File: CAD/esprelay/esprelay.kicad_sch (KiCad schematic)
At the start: 7 parts

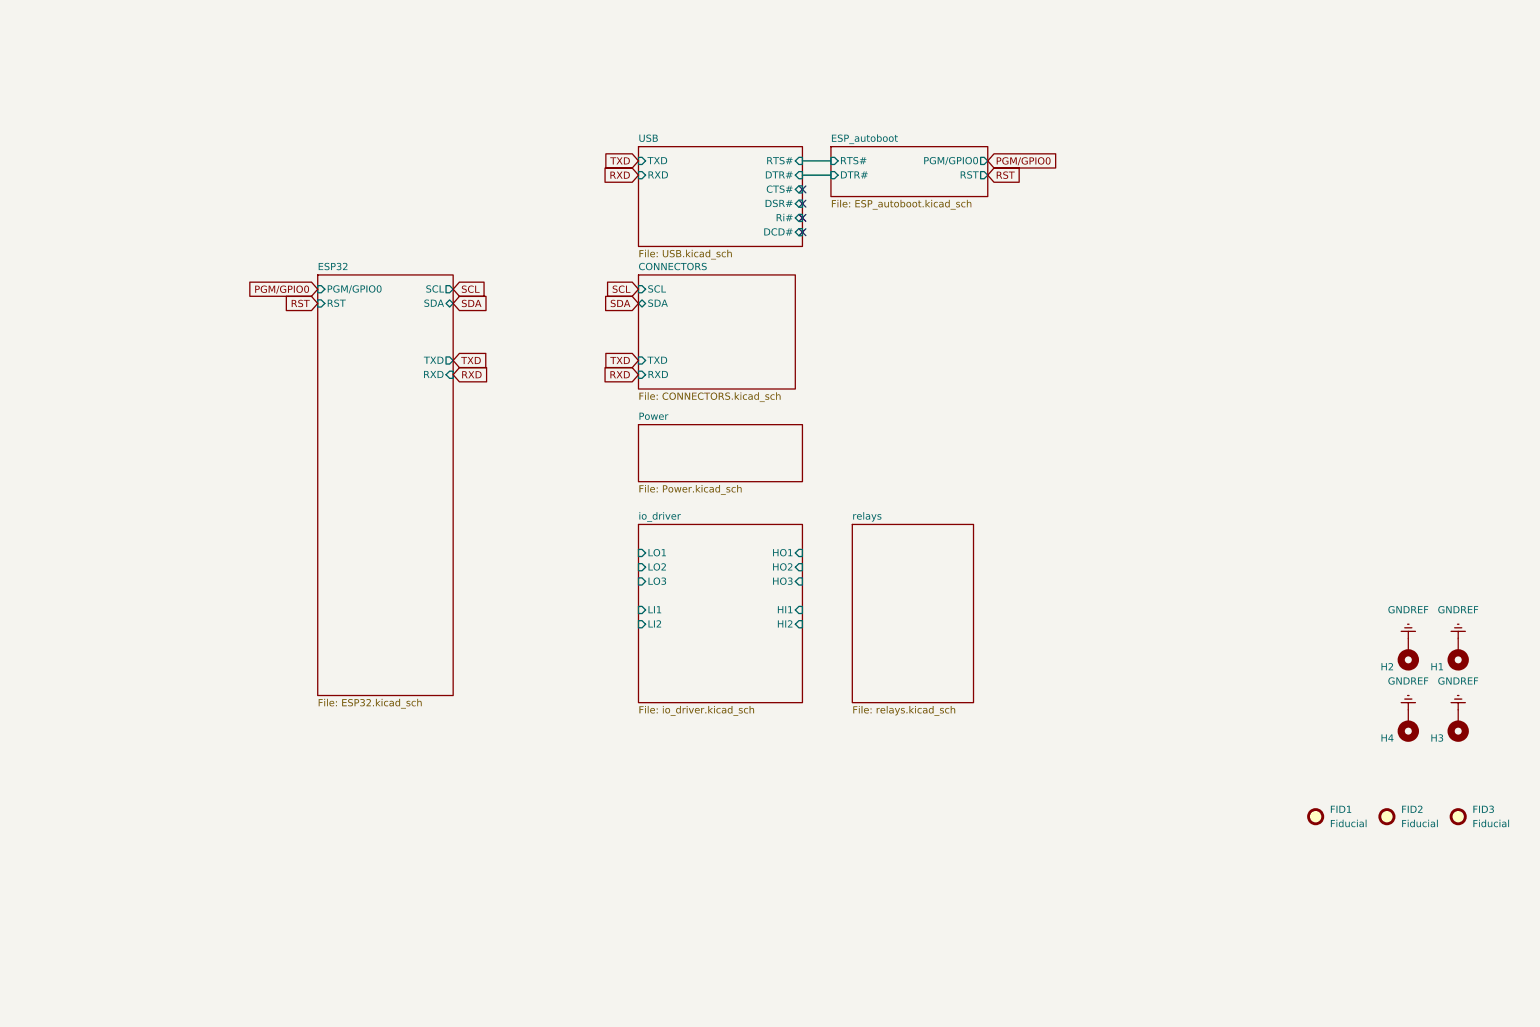
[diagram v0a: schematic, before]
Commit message: Feat: Changed module to ESP12F
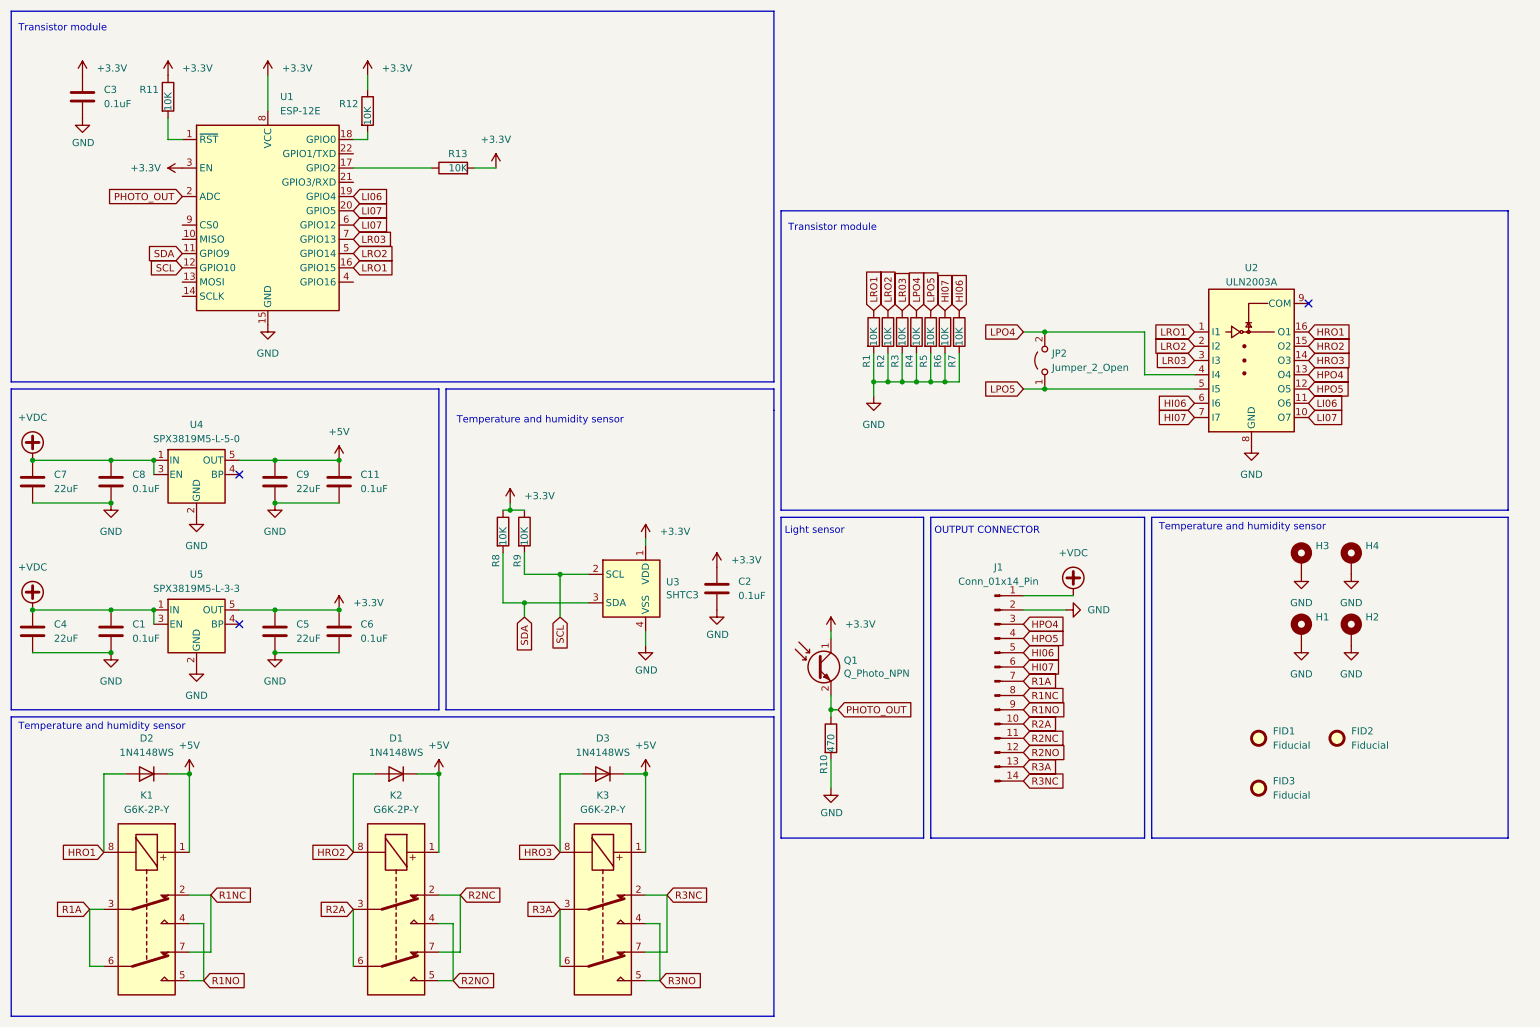
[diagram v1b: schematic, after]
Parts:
- added C1, C11, C2, C3, C6, C8: 0.1uF, Capacitor_SMD:C_0603_1608Metric, symbol Device:C
- added C4, C5, C7, C9: 22uF, Capacitor_SMD:C_0603_1608Metric, symbol Device:C
- added D1, D2, D3: 1N4148WS, Diode_SMD:D_SOD-323, symbol Diode:1N4148WS
- added J1: Conn_01x14_Pin, symbol Connector:Conn_01x14_Pin
- added JP2: Jumper_2_Open, Jumper:SolderJumper-2_P1.3mm_Open_TrianglePad1.0x1.5mm, symbol Jumper:Jumper_2_Open
- added K1, K2, K3: G6K-2P-Y, Relay_THT:Relay_DPDT_Omron_G6K-2P-Y, symbol Relay:G6K-2
- added Q1: Q_Photo_NPN, snapeda:TR8, symbol Device:Q_Photo_NPN
- added R1, R11, R12, R13, R2, R3, R4, R5, R6, R7, R8, R9: 10K, symbol Device:R
- added R10: 470, symbol Device:R
- added U1: ESP-12E, RF_Module:ESP-12E, symbol RF_Module:ESP-12E
- added U2: ULN2003A, Package_SO:SOIC-16_3.9x9.9mm_P1.27mm, symbol Transistor_Array:ULN2003A
- added U3: SHTC3, kicad:Sensirion_DFN-4-1EP_2x2mm_P1mm_EP0.7x1.6mm, symbol Sensor_Humidity:SHTC3
- added U4: SPX3819M5-L-5-0, Package_TO_SOT_SMD:SOT-23-5, symbol Regulator_Linear:SPX3819M5-L-5-0
- added U5: SPX3819M5-L-3-3, Package_TO_SOT_SMD:SOT-23-5, symbol Regulator_Linear:SPX3819M5-L-3-3
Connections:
- net SCL: now also R9.2, U1.12 (GPIO10), U3.2 (SCL)
- net SDA: now also R8.2, U1.11 (GPIO9), U3.3 (SDA)
- net GNDREF renamed GND
- net GND: now also C1.1, C11.2, C2.2, C3.2, C4.2, C5.2, C6.2, C7.2, C8.1, C9.2, J1.2 (Pin_2), R1.2, R10.2, R2.2, R3.2, R4.2, R5.2, R6.2, R7.2, U1.15 (GND), U2.8 (GND), U3.4 (VSS), U4.2 (GND), U5.2 (GND)
- new net: R11.2, U1.1 (~{RST})
- new net: R13.1, U1.17 (GPIO2)
- new net: R12.2, U1.18 (GPIO0)
- new net +3.3V: C2.1, C3.1, C5.1, C6.1, Q1.1 (C), R11.1, R12.1, R13.2, R8.1, R9.1, U1.3 (EN), U1.8 (VCC), U3.1 (VDD), U5.5 (OUT)
- new net +5V: C11.1, C9.1, D1.1 (K), D2.1 (K), D3.1 (K), K1.1, K2.1, K3.1, U4.5 (OUT)
- new net +VDC: C1.2, C4.1, C7.1, C8.2, J1.1 (Pin_1), U4.1 (IN), U4.3 (EN), U5.1 (IN), U5.3 (EN)
- new net HI06: J1.5 (Pin_5), R7.1, U2.6 (I6)
- new net HI07: J1.6 (Pin_6), R6.1, U2.7 (I7)
- new net HPO4: J1.3 (Pin_3), U2.13 (O4)
- new net HPO5: J1.4 (Pin_4), U2.12 (O5)
- new net HRO1: D2.2 (A), K1.8, U2.16 (O1)
- new net HRO2: D1.2 (A), K2.8, U2.15 (O2)
- new net HRO3: D3.2 (A), K3.8, U2.14 (O3)
- new net LI06: U1.19 (GPIO4), U2.11 (O6)
- new net LI07: U1.20 (GPIO5), U1.6 (GPIO12), U2.10 (O7)
- new net LPO4: JP2.2 (B), R4.1, U2.4 (I4)
- new net LPO5: JP2.1 (A), R5.1, U2.5 (I5)
- new net LR03: R3.1, U1.7 (GPIO13), U2.3 (I3)
- new net LRO1: R1.1, U1.16 (GPIO15), U2.1 (I1)
- new net LRO2: R2.1, U1.5 (GPIO14), U2.2 (I2)
- new net PHOTO_OUT: Q1.2 (E), R10.1, U1.2 (ADC)
- new net R1A: J1.7 (Pin_7), K1.3, K1.6
- new net R1NC: J1.8 (Pin_8), K1.2, K1.7
- new net R1NO: J1.9 (Pin_9), K1.4, K1.5
- new net R2A: J1.10 (Pin_10), K2.3, K2.6
- new net R2NC: J1.11 (Pin_11), K2.2, K2.7
- new net R2NO: J1.12 (Pin_12), K2.4, K2.5
- new net R3A: J1.13 (Pin_13), K3.3, K3.6
- new net R3NC: J1.14 (Pin_14), K3.2, K3.7
- new net R3NO: K3.4, K3.5
- no-connect marks 4 -> 3
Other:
- removed sheet CONNECTORS
- removed sheet ESP32
- removed sheet ESP_autoboot
- removed sheet Power
- removed sheet USB
- removed sheet io_driver
- removed sheet relays
- note added: "Light sensor"
- note added: "OUTPUT CONNECTOR"
- note added: "Temperature and humidity sensor"
- note added: "Transistor module"
- moved on the sheet: FID1, FID2, FID3, H1, H2, H3, H4

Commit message: Feat: Started Routing
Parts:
- removed JP2: Jumper_2_Open, Jumper:SolderJumper-2_P1.3mm_Open_TrianglePad1.0x1.5mm, symbol Jumper:Jumper_2_Open
- removed U1: ESP-12E, RF_Module:ESP-12E, symbol RF_Module:ESP-12E
- added J2: Conn_01x06_Pin, TestPoint:TestPoint_Pad_1.0x1.0mm_6pad, symbol Connector:Conn_01x06_Pin
- added JP1: Jumper_2_Open, Jumper:SolderJumper-2_P1.3mm_Open_TrianglePad1.0x1.5mm, symbol Jumper:Jumper_2_Open
- added U1: ESP-12F, RF_Module:ESP-12E, symbol RF_Module:ESP-12F
- J1: footprint (none) -> Connector_JST:JST_GH_SM12B-GHS-TB_1x12-1MP_P1.25mm_Horizontal
- R1, R10, R11, R12, R13, R2, R3, R4, R5, R6, R7, R8, R9: footprint (none) -> Resistor_SMD:R_0603_1608Metric
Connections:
- net +3.3V: now also J2.1 (Pin_1), JP1.2 (B), U1.3 (EN), U1.8 (VCC)
- net GND: now also J1.13 (Pin_13), J1.14 (Pin_14), J2.6 (Pin_6), U1.15 (GND)
- net HI06: now also J1.4 (Pin_4); no longer J1.5 (Pin_5)
- net HI07: now also J1.5 (Pin_5); no longer J1.6 (Pin_6)
- net LI06: now also U1.6 (GPIO12)
- net LI07: now also U1.20 (GPIO5)
- net LPO4: no longer U2.4 (I4)
- net LPO5: no longer U2.5 (I5)
- net LR03: now also U1.7 (GPIO13)
- net LRO1: now also U1.16 (GPIO15)
- net LRO2: now also U1.5 (GPIO14)
- net PHOTO_OUT: now also U1.2 (ADC)
- net R1A: now also J1.6 (Pin_6); no longer J1.7 (Pin_7)
- net R1NC: now also J1.7 (Pin_7); no longer J1.8 (Pin_8)
- net R1NO: now also J1.8 (Pin_8); no longer J1.9 (Pin_9)
- net R2A: now also J1.9 (Pin_9); no longer J1.10 (Pin_10)
- net R2NC: now also J1.10 (Pin_10); no longer J1.11 (Pin_11)
- net R2NO: no longer J1.12 (Pin_12)
- net R3A: now also J1.11 (Pin_11); no longer J1.13 (Pin_13)
- net R3NC: no longer J1.14 (Pin_14)
- net R3NO: now also J1.12 (Pin_12)
- net SCL: now also U1.12 (GPIO10)
- net SDA: now also U1.11 (GPIO9)
- net RST: now reaches R11.2
- net RST: now also J2.5 (Pin_5), U1.1 (~{RST}), U1.4 (GPIO16)
- net at R13.1: now also U1.17 (GPIO2)
- net BOOT: now reaches R12.2
- net BOOT: now also J2.4 (Pin_4), U1.18 (GPIO0)
- net +5V renamed VBUS
- net VBUS: now also JP1.1 (A)
- net HPO4 renamed HP45
- net HP45: now also U2.12 (O5); no longer J1.3 (Pin_3)
- removed net HPO5: J1.4 (Pin_4), U2.12 (O5)
- new net HPO45: J1.3 (Pin_3)
- new net LP45: U1.19 (GPIO4), U2.4 (I4), U2.5 (I5)
- new net RX: J2.3 (Pin_3), U1.21 (GPIO3/RXD)
- new net TX: J2.2 (Pin_2), U1.22 (GPIO1/TXD)
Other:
- note added: "Hardware"
- note added: "Linear Regulators"
- note added: "Relays"
- moved on the sheet: R12

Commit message: Feat: Pretty much complete
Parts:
- removed H1, H4: MountingHole_Pad, MountingHole:MountingHole_2.5mm, symbol Mechanical:MountingHole_Pad
- removed H2, H3: MountingHole_Pad, MountingHole:MountingHole_2.5mm_Pad_Via, symbol Mechanical:MountingHole_Pad
- removed R5: 10K, Resistor_SMD:R_0603_1608Metric, symbol Device:R
- added SW1: SW_SPST, Button_Switch_SMD:SW_SPST_B3U-1000P, symbol Switch:SW_SPST
- JP1: footprint Jumper:SolderJumper-2_P1.3mm_Open_TrianglePad1.0x1.5mm -> Resistor_SMD:R_0603_1608Metric
- Q1: footprint snapeda:TR8 -> LED_SMD:LED_0603_1608Metric
- U4: renamed from U3; footprint kicad:Sensirion_DFN-4-1EP_2x2mm_P1mm_EP0.7x1.6mm -> Sensor_Humidity:Sensirion_DFN-4-1EP_2x2mm_P1mm_EP0.7x1.6mm
- renumbered C7 to C1, C2 to C10, C4 to C2, C8 to C4, C1 to C5, C9 to C6, C5 to C7, C11 to C8, C6 to C9, D2 to D1, D1 to D2, FID3 to FID2, FID2 to FID3, J2 to J1, J1 to J2, R11 to R1, R4 to R10, R6 to R12, R7 to R13, R12 to R2, R13 to R3, R8 to R4, R9 to R5, R10 to R6, R1 to R7, R2 to R8, R3 to R9, U4 to U1, U5 to U2, U1 to U3, U2 to U5
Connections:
- net HPO45 is gone; now on net HI1: J2.3 (Pin_3)
- net BOOT: now also SW1.1 (A)
- net GND: now also SW1.2 (B)
- net R2NC: no longer J2.10 (Pin_10)
- net R2NO: now also J2.10 (Pin_10)
- net HI06 renamed HI1
- net HI1: no longer J2.4 (Pin_4)
- net HI07 renamed HI2
- net HI2: now also J2.4 (Pin_4); no longer J2.5 (Pin_5)
- net HP45 renamed RO2
- net RO2: now also D2.2 (A), K2.8; no longer U5.12 (O5)
- net HRO1 renamed RO1
- net RO1: now also U5.14 (O3); no longer U5.16 (O1)
- removed net HRO2: D2.2 (A), K2.8, U5.15 (O2)
- net HRO3 renamed RO3
- net RO3: now also U5.12 (O5); no longer U5.14 (O3)
- net LI06 renamed GPIO12
- net GPIO12: now also R8.1, U5.3 (I3); no longer U5.11 (O6)
- net LI07 renamed GPIO15
- net GPIO15: now also U3.16 (GPIO15); no longer U3.20 (GPIO5)
- removed net LP45: U3.19 (GPIO4), U5.4 (I4), U5.5 (I5)
- net LPO4 renamed GPIO5
- net GPIO5: now also U3.20 (GPIO5), U5.5 (I5)
- removed net LR03: R9.1, U3.7 (GPIO13), U5.3 (I3)
- net LRO1 renamed GPIO13
- net GPIO13: now also U3.7 (GPIO13), U5.2 (I2); no longer U3.16 (GPIO15)
- removed net LRO2: R8.1, U3.5 (GPIO14), U5.2 (I2)
- new net GPIO14: R9.1, U3.5 (GPIO14), U5.4 (I4)
- new net GPIO4: U3.19 (GPIO4), U5.11 (O6)
- new net HO1: J2.5 (Pin_5), U5.15 (O2), U5.16 (O1)
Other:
- moved on the sheet: R12, R13

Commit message: Feat: Fixed lcsc product numbers
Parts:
- C1, C2, C6, C7: INFO DIGIKEY -> (none); LCSC (none) -> C96446
- C10, C3, C4, C5, C8, C9: INFO DIGIKEY -> (none); LCSC (none) -> C14663
- D1, D2, D3: LCSC (none) -> C2128
- J2: LCSC (none) -> C265421
- K1, K2, K3: LCSC (none) -> C80087
- R1, R10, R2, R3, R4, R5, R7, R8, R9: LCSC (none) -> C25804
- R11: renamed from R12; LCSC (none) -> C25804
- R12: renamed from R13; LCSC (none) -> C25804
- R6: LCSC (none) -> C23179
- SW1: LCSC (none) -> C231329; LSC C231329 -> (none)
- U1: LCSC (none) -> C13417
- U2: LCSC (none) -> C9055
- U3: LCSC (none) -> C82891
- U5: LCSC (none) -> C7512
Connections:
- net GND: now also J2.MP (Pin_14); no longer J2.13 (Pin_13), J2.14 (Pin_14)

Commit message: Feat: Finished silkscreen
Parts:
- C1, C2, C6, C7: LCSC C96446 -> (none); LCSC Part # (none) -> C96446; MPN CL21A226MOCLRNC -> (none); Supplier Part Number 1276-6780-6-ND -> (none)
- C10, C3, C4, C5, C8, C9: LCSC C14663 -> (none); LCSC Part # (none) -> C14663; MPN 06035C104KAT4A -> (none); Supplier Part Number 478-10346-1-ND -> (none)
- D1, D2, D3: LCSC C2128 -> (none); LCSC Part # (none) -> C2128
- J2: LCSC C265421 -> (none); LCSC Part # (none) -> C265421
- K1, K2, K3: LCSC C80087 -> (none); LCSC Part # (none) -> C80087
- Q1: LCSC C146233 -> (none); LCSC Part # (none) -> C146233
- R1, R10, R11, R12, R2, R3, R4, R5, R7, R8, R9: LCSC C25804 -> (none); LCSC Part # (none) -> C25804
- R6: LCSC C23179 -> (none); LCSC Part # (none) -> C23179
- SW1: LCSC C231329 -> (none); LCSC Part # (none) -> C231329
- U1: LCSC C13417 -> (none); LCSC Part # (none) -> C13417
- U2: LCSC C9055 -> (none); LCSC Part # (none) -> C9055
- U3: LCSC C82891 -> (none); LCSC Part # (none) -> C82891
- U4: LCSC C194656 -> (none); LCSC Part # (none) -> C194656
- U5: LCSC C7512 -> (none); LCSC Part # (none) -> C7512

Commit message: Feat: JLC purchase
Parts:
- added D4: KT-0603R, LED_SMD:LED_0603_1608Metric, symbol Device:LED
- added R13: 470, Resistor_SMD:R_0603_1608Metric, symbol Device:R
- J2: value Conn_01x14_Pin -> SM12B-GHS-TB(LF)(SN)
- JP1: LCSC Part # (none) -> C21189; now not fitted
- SW1: footprint Button_Switch_SMD:SW_SPST_B3U-1000P -> Button_Switch_SMD:SW_SPST_TS-1088-AR; LCSC Part # C231329 -> C720477
- U5: value ULN2003A -> TBD62003AFWG; LCSC Part # C7512 -> C114084
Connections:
- net +3.3V: now also D4.2 (A)
- net GPIO15: now also R10.1, U5.5 (I5); no longer U5.10 (O7)
- net GPIO5: now also U5.10 (O7); no longer R10.1, U5.5 (I5)
- net GPIO2: now reaches R3.1, U3.17 (GPIO2)
- net GPIO2: now also R13.2
- new net: D4.1 (K), R13.1
- no-connect marks 3 -> 7
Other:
- moved on the sheet: R3

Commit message: Feat: Readme and documentation work
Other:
- note added: "MCU"
- note added: "Output connector"
- note added: "Programming header"
- note removed: "OUTPUT CONNECTOR"
- company: (none) -> Drawn by FNB
- title: (none) -> ESPRelay
- moved on the sheet: FID1, FID2, FID3, R4, R5, U5

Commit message: Simplification
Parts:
- removed C10: 0.1uF, Capacitor_SMD:C_0603_1608Metric, symbol Device:C
- removed D3: 1N4148WS, Diode_SMD:D_SOD-323, symbol Diode:1N4148WS
- removed D4: KT-0603R, LED_SMD:LED_0603_1608Metric, symbol Device:LED
- removed FID1, FID2, FID3: Fiducial, Fiducial:Fiducial_1mm_Mask2mm, symbol Mechanical:Fiducial
- removed JP1: Jumper_2_Open, Resistor_SMD:R_0603_1608Metric, symbol Jumper:Jumper_2_Open
- removed K3: G6K-2P-Y, Relay_THT:Relay_DPDT_Omron_G6K-2P-Y, symbol Relay:G6K-2
- removed Q1: Q_Photo_NPN, LED_SMD:LED_0603_1608Metric, symbol Device:Q_Photo_NPN
- removed R13: 470, Resistor_SMD:R_0603_1608Metric, symbol Device:R
- removed R4, R5: 10K, Resistor_SMD:R_0603_1608Metric, symbol Device:R
- removed SW1: SW_SPST, Button_Switch_SMD:SW_SPST_TS-1088-AR, symbol Switch:SW_SPST
- removed U1: SPX3819M5-L-5-0, Package_TO_SOT_SMD:SOT-23-5, symbol Regulator_Linear:SPX3819M5-L-5-0
- removed U2: SPX3819M5-L-3-3, Package_TO_SOT_SMD:SOT-23-5, symbol Regulator_Linear:SPX3819M5-L-3-3
- removed U4: SHTC3, Sensor_Humidity:Sensirion_DFN-4-1EP_2x2mm_P1mm_EP0.7x1.6mm, symbol Sensor_Humidity:SHTC3
- added U1: DS8242-33S5, Package_TO_SOT_SMD:SOT-23-5, symbol Regulator_Linear:DS8242
- added U2: DS8242-50S3, Package_TO_SOT_SMD:SOT-23-5, symbol Regulator_Linear:DS8242
- C1, C2, C6, C7: value 22uF -> 1uF; footprint Capacitor_SMD:C_0603_1608Metric -> Capacitor_SMD:C_0402_1005Metric; LCSC Part # C96446 -> C52923
- C3, C4, C5, C8, C9: footprint Capacitor_SMD:C_0603_1608Metric -> Capacitor_SMD:C_0402_1005Metric; LCSC Part # C14663 -> C307331
- R1, R10, R11, R12, R2, R7, R8, R9: footprint Resistor_SMD:R_0603_1608Metric -> Resistor_SMD:R_0402_1005Metric; LCSC Part # C25804 -> C25744
- R3: value 10K -> 13.7k; footprint Resistor_SMD:R_0603_1608Metric -> Resistor_SMD:R_0402_1005Metric; LCSC Part # C25804 -> C25854
- R6: value 470 -> 316k; footprint Resistor_SMD:R_0603_1608Metric -> Resistor_SMD:R_0402_1005Metric; LCSC Part # C23179 -> C25777
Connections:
- net R3A is gone; now on net R2CO: J2.11 (Pin_11)
- net R3NO is gone; now on net R2NO: J2.12 (Pin_12)
- net RO3 is gone; now on net RO2: U5.12 (O5)
- net +3.3V: now also U1.5 (OUT); no longer R3.2
- net +VDC: now also R6.1, U1.1 (IN), U1.3 (NC), U2.1 (IN), U2.3 (NC)
- net GND: now also R3.2, U1.2 (GND), U2.2 (GND); no longer R6.2
- net R1NO: now also J2.9 (Pin_9); no longer J2.8 (Pin_8)
- net R2NC: now also J2.10 (Pin_10)
- net R2NO: no longer J2.10 (Pin_10)
- net RO1: now also U5.13 (O4); no longer U5.14 (O3)
- net RO2: no longer U5.13 (O4)
- net VBUS: now also U2.5 (OUT)
- net GPIO2: no longer names the net of U3.17 (GPIO2)
- net GPIO2: no longer R3.1
- net PHOTO_OUT renamed ADC
- net ADC: now also R3.1, R6.2; no longer R6.1
- net R1A renamed R1CO
- net R1CO: now also J2.8 (Pin_8); no longer J2.6 (Pin_6)
- net R2A renamed R2CO
- net R2CO: no longer J2.9 (Pin_9)
- net SCL: no longer names the net of U3.12 (GPIO10)
- net SDA: no longer names the net of U3.11 (GPIO9)
- new net HO2: J2.6 (Pin_6), U5.14 (O3)
- no-connect marks 7 -> 10
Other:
- note added: "Voltage sensor"
- note removed: "Hardware"
- note removed: "Light sensor"
- note removed: "Temperature and humidity sensor"
- moved on the sheet: J1, J2, R10, R11, R12, R6, R7, R8, R9, U5
